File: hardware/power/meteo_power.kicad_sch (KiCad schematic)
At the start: 18 parts, among them J1 PV-12W 12V 1A, U1 CN3791 12V MPPT, U2 MT3608 -> 5.0V, U3 ESP32-H2-DevKitM-1, U4 BMP388 0x76, U5 MLX90614 0x5A

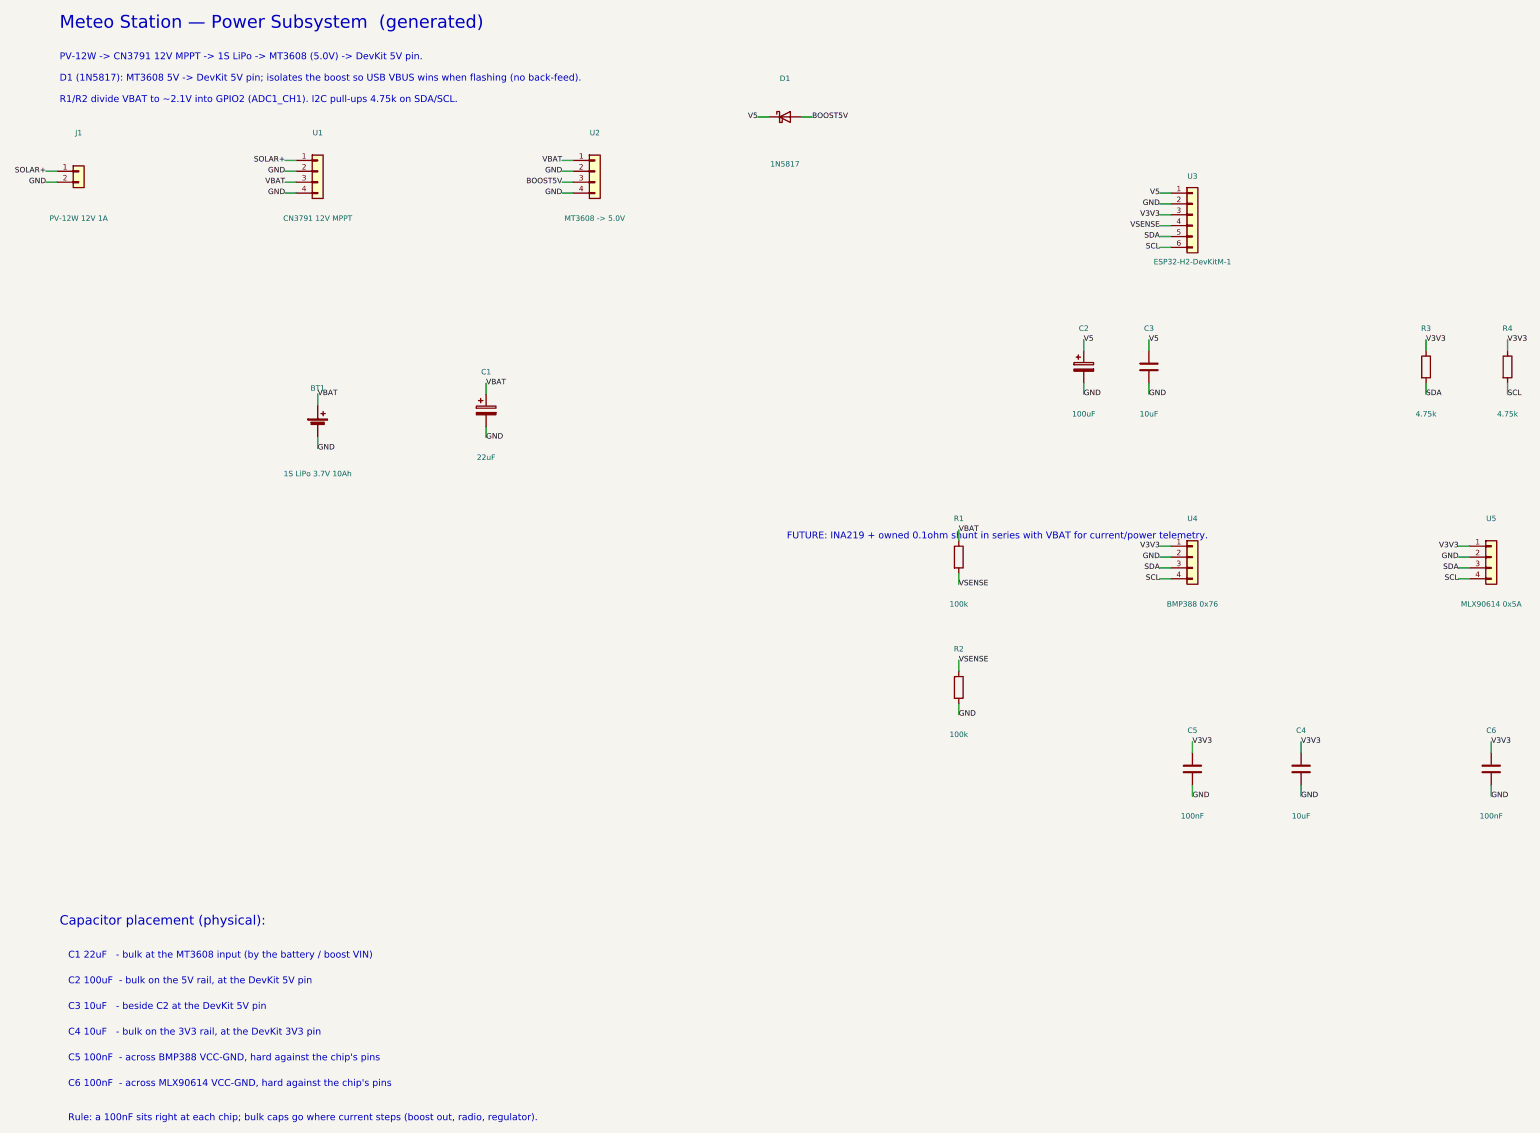
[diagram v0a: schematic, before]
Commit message: feat(power): add dual INA219 current/power monitoring
Two INA219 breakouts (INA219B, on-board 0.1ohm shunt, +/-3.2A) on the shared
I2C0 bus replace the GPIO2 analog battery divider:

- U6 @ 0x40: high-side on the PV feed (SOLAR+ -> SOLAR_CHG) -> solar harvest
  current + panel voltage.
- U7 @ 0x41: high-side on the battery->boost feed (VBAT -> VLOAD) -> system
  load current + battery voltage (INA219 bus register, more accurate than the
  H2 SAR ADC).

R1/R2 + the VSENSE net are dropped; the DevKit connector shrinks 6->5 pins and
GPIO2/ADC1_CH1 is freed as a spare. C1 bulk moves to VLOAD (boost VIN, after the
U7 shunt). Generated via gen_power_sch.py; ERC clean (0 violations).

Also gitignores KiCad runtime cruft (*.lck, _autosave-*) and drops the two
previously-committed autosave/lock files.

Co-Authored-By: Claude Opus 4.8 (1M context) <noreply@anthropic.com>
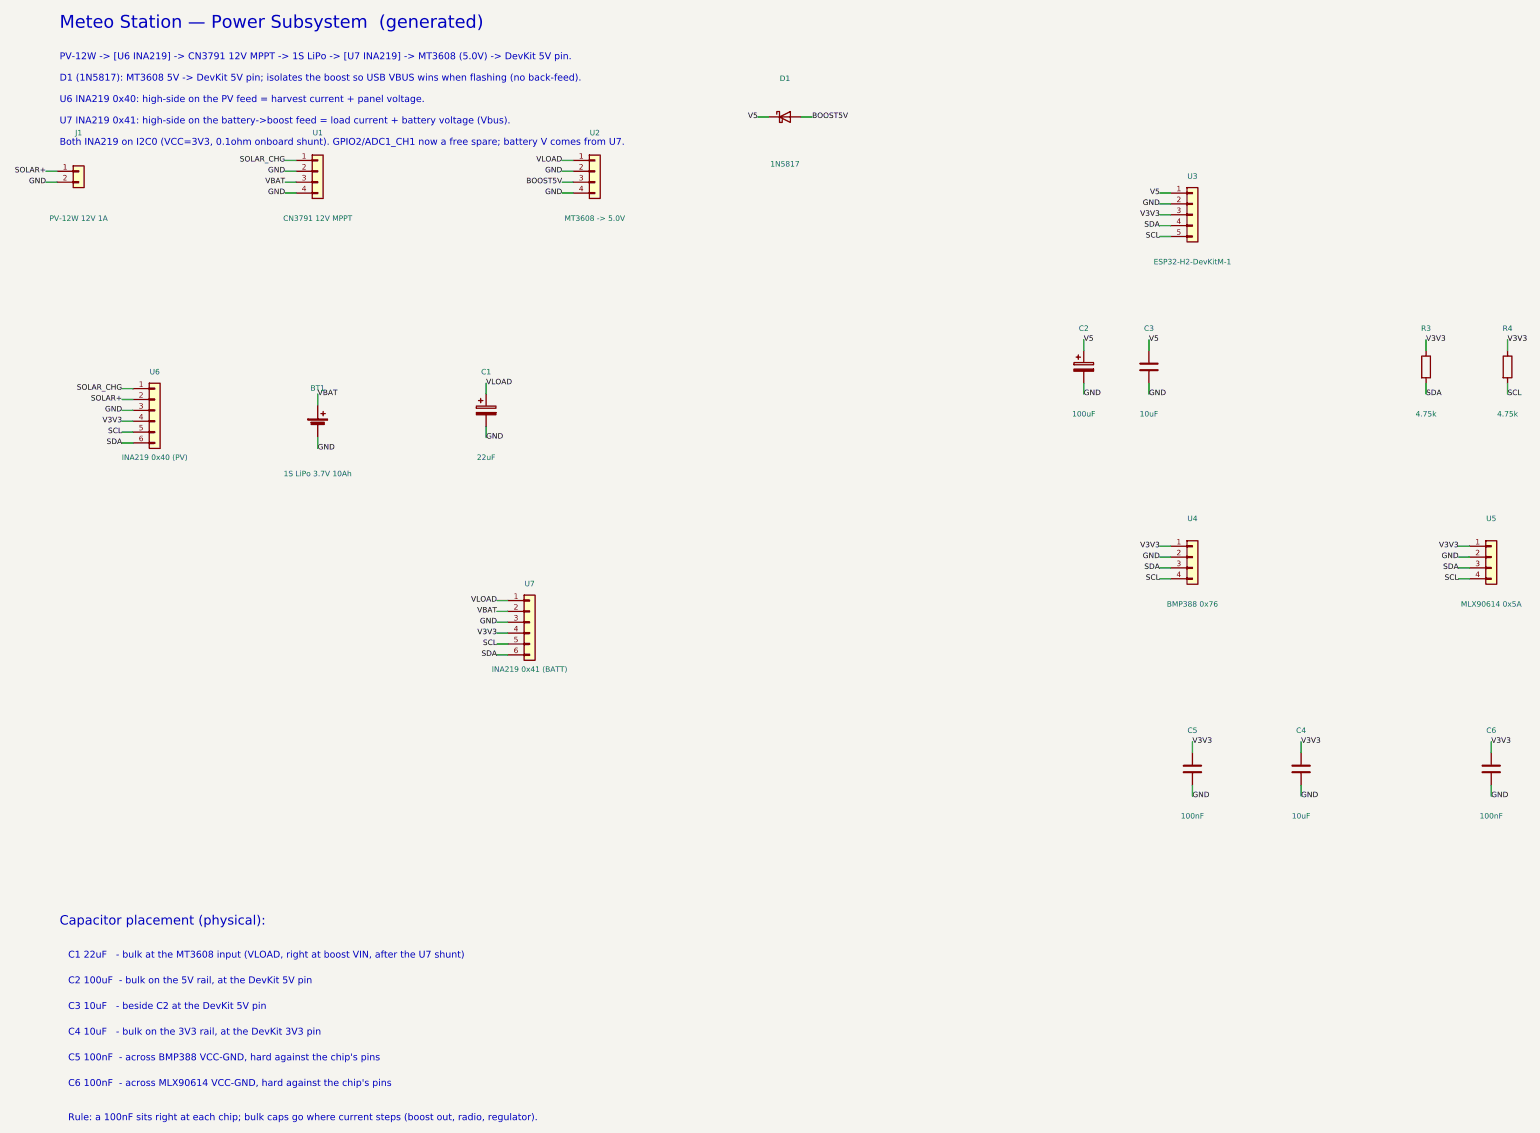
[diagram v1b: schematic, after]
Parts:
- removed R1, R2: 100k, symbol Device:R
- removed U3: ESP32-H2-DevKitM-1, symbol Connector_Generic:Conn_01x06
- added U3: ESP32-H2-DevKitM-1, symbol Connector_Generic:Conn_01x05
- added U6: INA219 0x40 (PV), symbol Connector_Generic:Conn_01x06
- added U7: INA219 0x41 (BATT), symbol Connector_Generic:Conn_01x06
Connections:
- net GND: now also U3.2 (Pin_2), U6.3 (Pin_3), U7.3 (Pin_3)
- net SCL: now also U3.5 (Pin_5), U6.5 (Pin_5), U7.5 (Pin_5)
- net SDA: now also U3.4 (Pin_4), U6.6 (Pin_6), U7.6 (Pin_6)
- net SOLAR+: now also U6.2 (Pin_2); no longer U1.1 (Pin_1)
- net V3V3: now also U3.3 (Pin_3), U6.4 (Pin_4), U7.4 (Pin_4)
- net V5: now also U3.1 (Pin_1)
- net VBAT: now also U7.2 (Pin_2); no longer C1.1, U2.1 (Pin_1)
- new net SOLAR_CHG: U1.1 (Pin_1), U6.1 (Pin_1)
- new net VLOAD: C1.1, U2.1 (Pin_1), U7.1 (Pin_1)
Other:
- note added: "Both INA219 on I2C0 (VCC=3V3, 0.1ohm onboard shunt). GPIO2/ADC1_CH1 now a free spare; battery V comes from U7."
- note added: "C1 22uF - bulk at the MT3608 input (VLOAD, right at boost VIN, after the U7 shunt)"
- note added: "PV-12W -> [U6 INA219] -> CN3791 12V MPPT -> 1S LiPo -> [U7 INA219] -> MT3608 (5.0V) -> DevKit 5V pin."
- note added: "U6 INA219 0x40: high-side on the PV feed = harvest current + panel voltage."
- note added: "U7 INA219 0x41: high-side on the battery->boost feed = load current + battery voltage (Vbus)."
- note removed: "C1 22uF - bulk at the MT3608 input (by the battery / boost VIN)"
- note removed: "FUTURE: INA219 + owned 0.1ohm shunt in series with VBAT for current/power telemetry."
- note removed: "PV-12W -> CN3791 12V MPPT -> 1S LiPo -> MT3608 (5.0V) -> DevKit 5V pin."
- note removed: "R1/R2 divide VBAT to ~2.1V into GPIO2 (ADC1_CH1). I2C pull-ups 4.75k on SDA/SCL."

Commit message: fix(power): correct BMP388 address and add BME280/VEML7700 to the sheet
The power sheet's I2C section was stale: U4 was labelled 0x76 (that's the BME280's
address) and the BME280 + VEML7700 the firmware actually drives weren't shown at all.

- U4 BMP388: 0x76 -> 0x77 (matches the firmware / CLAUDE.md).
- Add U8 BME280 (0x76) and U9 VEML7700 (0x10) to the shared I2C0 bus.

Both new parts are breakout modules with onboard decoupling, so no external 100nF is
added (noted on the sheet); only the bare MLX90614 keeps its discrete cap. Regenerated
via gen_power_sch.py; ERC clean (0 violations).

Co-Authored-By: Claude Opus 4.8 (1M context) <noreply@anthropic.com>
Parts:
- added U8: BME280 0x76, symbol Connector_Generic:Conn_01x04
- added U9: VEML7700 0x10, symbol Connector_Generic:Conn_01x04
- U4: value BMP388 0x76 -> BMP388 0x77
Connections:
- net GND: now also U8.2 (Pin_2), U9.2 (Pin_2)
- net SCL: now also U8.4 (Pin_4), U9.4 (Pin_4)
- net SDA: now also U8.3 (Pin_3), U9.3 (Pin_3)
- net V3V3: now also U8.1 (Pin_1), U9.1 (Pin_1)
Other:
- note added: "U8 BME280 & U9 VEML7700 are breakout modules (onboard decoupling); only the bare MLX90614 needs its external 100nF."
